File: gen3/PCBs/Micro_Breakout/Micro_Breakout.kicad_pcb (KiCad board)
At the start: 4 copper layers, 0 parts

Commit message: microcontroller breakout board completed!!
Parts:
- added C1: 10uF, Capacitor_SMD:C_0805_2012Metric_Pad1.18x1.45mm_HandSolder, F.Cu at (83.0, 73.5)
- added C12: 10uF, Capacitor_SMD:C_0805_2012Metric_Pad1.18x1.45mm_HandSolder, F.Cu at (84.5, 85.5)
- added C13: 10uF, Capacitor_SMD:C_0805_2012Metric_Pad1.18x1.45mm_HandSolder, F.Cu at (83.5, 89.5)
- added C14: 1uF, Capacitor_SMD:C_0805_2012Metric_Pad1.18x1.45mm_HandSolder, F.Cu at (87.0, 89.5)
- added C15: 10uF, Capacitor_SMD:C_0805_2012Metric_Pad1.18x1.45mm_HandSolder, F.Cu at (76.0, 81.0)
- added C2: 1uF, Capacitor_SMD:C_0805_2012Metric_Pad1.18x1.45mm_HandSolder, F.Cu at (86.0, 73.5)
- added H6: MountingHole, MountingHole:MountingHole_4.3mm_M4, F.Cu at (64.0, 54.5)
- added H7: MountingHole, MountingHole:MountingHole_4.3mm_M4, F.Cu at (64.0, 128.5)
- added H8: MountingHole, MountingHole:MountingHole_4.3mm_M4, F.Cu at (178.5, 54.5)
- added H9: MountingHole, MountingHole:MountingHole_4.3mm_M4, F.Cu at (178.5, 128.5)
- added J1: BlueRobotics Depth Sensor, Imported_Footprints:CONN_SD-43045-005_04_MOL, F.Cu at (134.5, 57.1)
- added J10: Kill Switch, Imported_Footprints:CONN_SD-43045-005_02_MOL, F.Cu at (141.3, 73.9)
- added J11: StarOddi CTD Comms, Imported_Footprints:CONN_SD-43045-005_04_MOL, F.Cu at (147.5, 57.1)
- added J12: LED1, Imported_Footprints:CONN_SD-43045-005_02_MOL, F.Cu at (150.8, 74.0)
- added J13: LED2, Imported_Footprints:CONN_SD-43045-005_02_MOL, F.Cu at (160.3, 74.0)
- added J14: Leak Sensor, Connector_PinHeader_2.54mm:PinHeader_1x03_P2.54mm_Vertical, F.Cu at (155.0, 57.1)
- added J15: Extra I2C #3, Imported_Footprints:CONN_SD-43045-005_04_MOL, F.Cu at (98.0, 88.5)
- added J16: Extra I2C #6, Imported_Footprints:CONN_SD-43045-005_04_MOL, F.Cu at (98.0, 121.5)
- added J17: Extra I2C #5, Imported_Footprints:CONN_SD-43045-005_04_MOL, F.Cu at (98.0, 110.5)
- added J18: Extra I2C #4, Imported_Footprints:CONN_SD-43045-005_04_MOL, F.Cu at (98.0, 99.5)
- added J19: GND Line, Connector_PinHeader_2.54mm:PinHeader_1x10_P2.54mm_Vertical, F.Cu at (74.0, 127.3)
- added J2: Interconnect, Imported_Footprints:SULLINS_SBH11-PBPC-D05-ST-BK, F.Cu at (153.9, 89.3)
- added J20: 3.3V Line, Connector_PinHeader_2.54mm:PinHeader_1x10_P2.54mm_Vertical, F.Cu at (78.0, 127.3)
- added J21: 5V Line, Connector_PinHeader_2.54mm:PinHeader_1x10_P2.54mm_Vertical, F.Cu at (82.0, 127.2)
- added J22: Extra SPI #1, Imported_Footprints:CONN_SD-43045-005_06_MOL, F.Cu at (119.5, 57.0)
- added J23: Extra SPI #2, Imported_Footprints:CONN_SD-43045-005_06_MOL, F.Cu at (119.5, 74.0)
- added J24: Extra SPI #3, Imported_Footprints:CONN_SD-43045-005_06_MOL, F.Cu at (119.5, 91.6)
- added J25: Secondary UART, Imported_Footprints:CONN_SD-43045-005_04_MOL, F.Cu at (134.8, 91.5)
- added J3: External Battery, Connector_AMASS:AMASS_XT60PW-F_1x02_P7.20mm_Horizontal, F.Cu at (83.2, 57.8)
- added J4: Conn_01x24, Connector_PinHeader_2.54mm:PinHeader_1x24_P2.54mm_Vertical, F.Cu at (168.1, 103.6)
- added J5: External I2C, Connector_AMASS:AMASS_XT30PW-F_1x02_P2.50mm_Horizontal, F.Cu at (94.5, 57.6)
- added J6: Conn_01x24, Connector_PinHeader_2.54mm:PinHeader_1x24_P2.54mm_Vertical, F.Cu at (168.0, 126.1)
- added J7: Extra I2C #1, Imported_Footprints:CONN_SD-43045-005_04_MOL, F.Cu at (98.0, 66.5)
- added J8: Extra I2C #2, Imported_Footprints:CONN_SD-43045-005_04_MOL, F.Cu at (98.0, 77.5)
- added J9: Lumen PWM, Imported_Footprints:CONN_SD-43045-005_02_MOL, F.Cu at (131.8, 73.9)
- added Q7: L78M05ABDT-TR, robosub_footprints:TO-252-2_L6.5-W6.1-P4.58-LS10.0-TL, F.Cu at (76.0, 74.0)
- added R1: 0R, Resistor_SMD:R_0805_2012Metric_Pad1.20x1.40mm_HandSolder, F.Cu at (83.0, 96.0)
- added R10: 10k, Resistor_SMD:R_0805_2012Metric_Pad1.20x1.40mm_HandSolder, F.Cu at (104.5, 112.0)
- added R11: 10k, Resistor_SMD:R_0805_2012Metric_Pad1.20x1.40mm_HandSolder, F.Cu at (104.5, 109.0)
- added R2: 10k, Resistor_SMD:R_0805_2012Metric_Pad1.20x1.40mm_HandSolder, F.Cu at (83.0, 99.0)
- added R3: 10k, Resistor_SMD:R_0805_2012Metric_Pad1.20x1.40mm_HandSolder, F.Cu at (87.0, 98.0)
- added R4: 10k, Resistor_SMD:R_0805_2012Metric_Pad1.20x1.40mm_HandSolder, F.Cu at (86.0, 68.5)
- added R5: 10k, Resistor_SMD:R_0805_2012Metric_Pad1.20x1.40mm_HandSolder, F.Cu at (83.0, 68.5)
- added R6: 10k, Resistor_SMD:R_0805_2012Metric_Pad1.20x1.40mm_HandSolder, F.Cu at (104.5, 121.0)
- added R7: 10k, Resistor_SMD:R_0805_2012Metric_Pad1.20x1.40mm_HandSolder, F.Cu at (104.5, 118.0)
- added R8: 10k, Resistor_SMD:R_0805_2012Metric_Pad1.20x1.40mm_HandSolder, F.Cu at (104.5, 115.0)
- added U15: AMS1117-3.3, Package_TO_SOT_SMD:SOT-223-3_TabPin2, F.Cu at (77.0, 88.0)
- added U2: MCP9808_MSOP, Package_SO:MSOP-8_3x3mm_P0.65mm, F.Cu at (84.5, 78.5)
- added U4: BME280, Package_LGA:Bosch_LGA-8_2.5x2.5mm_P0.65mm_ClockwisePinNumbering, F.Cu at (77.0, 97.5)
- added U6: Teensy4.1, Imported_Footprints:Teensy41, F.Cu at (138.8, 114.9)
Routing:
- net GND: track 0.00 -> 379.9 mm
- net +3.3V: track 0.00 -> 364.2 mm, vias 0 -> 7
- net I2C1_SDA: track 0.00 -> 259.3 mm, vias 0 -> 2
- net I2C1_SCL: track 0.00 -> 233.5 mm
- net UART_TX2: track 0.00 -> 214.5 mm
- net +5V: track 0.00 -> 176.1 mm, vias 0 -> 2
- net SPI_SCK: track 0.00 -> 164.6 mm
- net UART_RX2: track 0.00 -> 115.3 mm, vias 0 -> 4
- net UART_TX1: track 0.00 -> 114.2 mm
- net UART_RX1: track 0.00 -> 110.1 mm
- net I2C2_SDA: track 0.00 -> 97.5 mm, vias 0 -> 1
- net SPI_MISO: track 0.00 -> 88.4 mm, vias 0 -> 6
- net SPI_CS3: track 0.00 -> 83.3 mm
- net I2C2_SCL: track 0.00 -> 81.7 mm
- net SPI_MOSI: track 0.00 -> 72.9 mm, vias 0 -> 3
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- added copper zone on B.Cu, net GND
- added copper zone on F.Cu, net GND
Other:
- board outline added: 123.5 x 83 mm
- copper layers 4 -> 2
- board text added: "/\ /**\ /****\ /******\ ||"
- board text added: "3.3V"
- board text added: "5V"
- board text added: "BlueRobotics Depth"
- board text added: "By: Ryota Sato"
- board text added: "Extra I2C"
- board text added: "Extra UART"
- board text added: "GND"
- board text added: "Interconnect"
- board text added: "Kill Switch"
- board text added: "LED1"
- board text added: "LED2"
- board text added: "Leak Sensor"
- board text added: "Microcontroller Breakout Board"
- board text added: "SPI #1"
- board text added: "SPI #2"
- board text added: "SPI #3"
- board text added: "StarOddi"

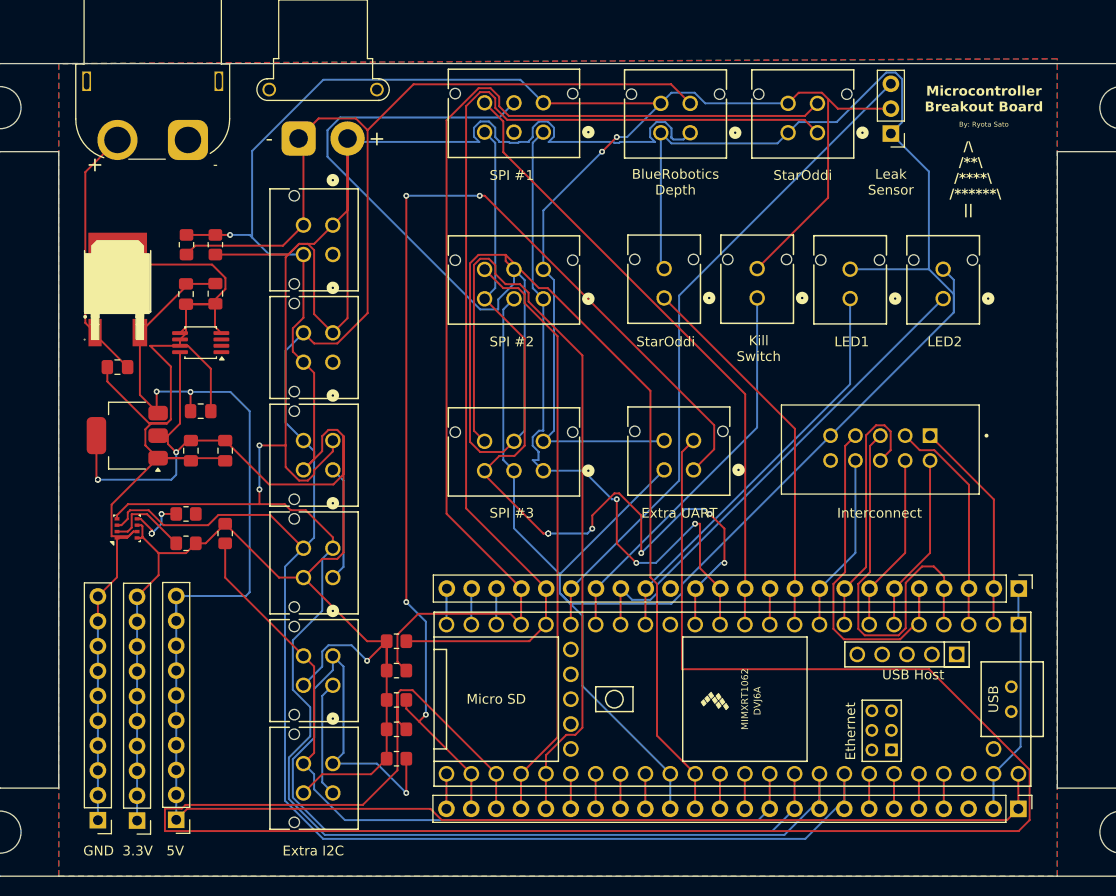
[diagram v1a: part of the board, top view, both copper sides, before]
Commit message: fixed pinout for ribbon
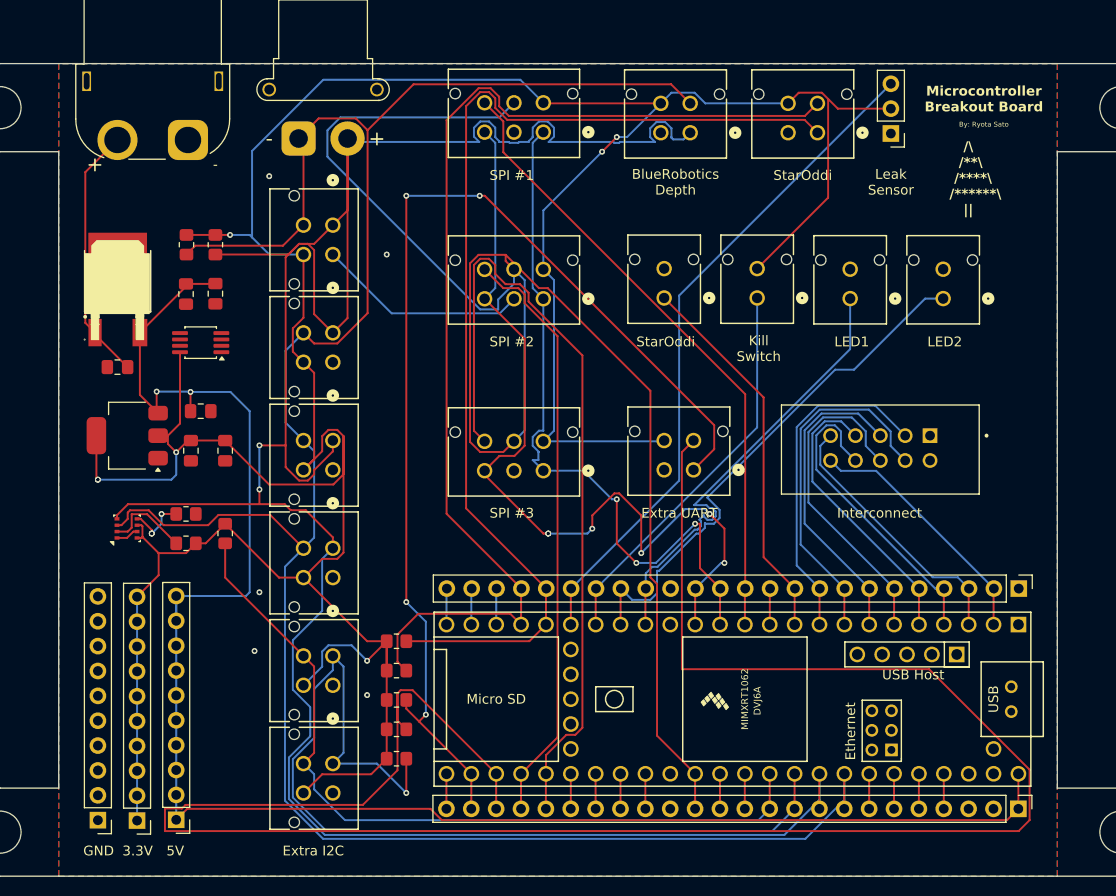
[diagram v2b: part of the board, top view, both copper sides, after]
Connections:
- J2 pad 1: PWM0 -> unconnected-(J2-Pad1)
- J2 pad 10: unconnected-(J2-Pad10) -> PWM0
- J2 pad 2: PWM4 -> GND
- J2 pad 3: PWM1 -> PWM7
- J2 pad 4: PWM5 -> PWM6
- J2 pad 5: PWM2 -> PWM5
- J2 pad 6: PWM6 -> PWM4
- J2 pad 8: PWM7 -> PWM2
- J2 pad 9: GND -> PWM1
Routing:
- net GND: track 379.9 -> 24.0 mm, vias 0 -> 5
- net PWM7: track 18.3 -> 34.4 mm
- net PWM4: track 18.3 -> 34.0 mm
- net PWM5: track 18.3 -> 32.0 mm
- net PWM6: track 26.9 -> 36.4 mm
- net PWM2: track 40.7 -> 32.1 mm
- net PWM3: track 37.6 -> 29.6 mm
- net PWM1: track 22.9 -> 27.5 mm
- net Dled1: track 42.0 -> 46.5 mm
- net Dled2: track 50.3 -> 54.5 mm
- net PWM0: track 22.0 -> 25.8 mm
- net I2C1_SDA: vias 2 -> 3

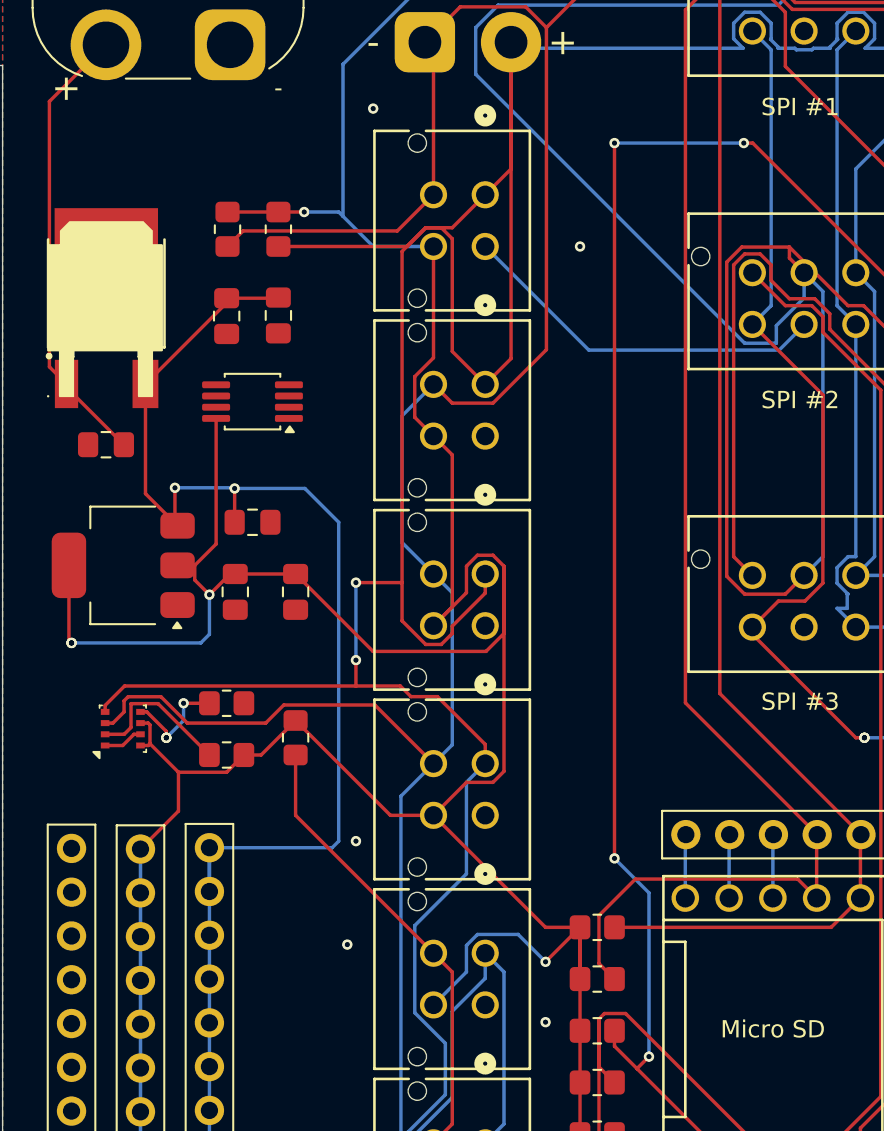
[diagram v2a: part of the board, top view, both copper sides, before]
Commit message: fixed GND plane
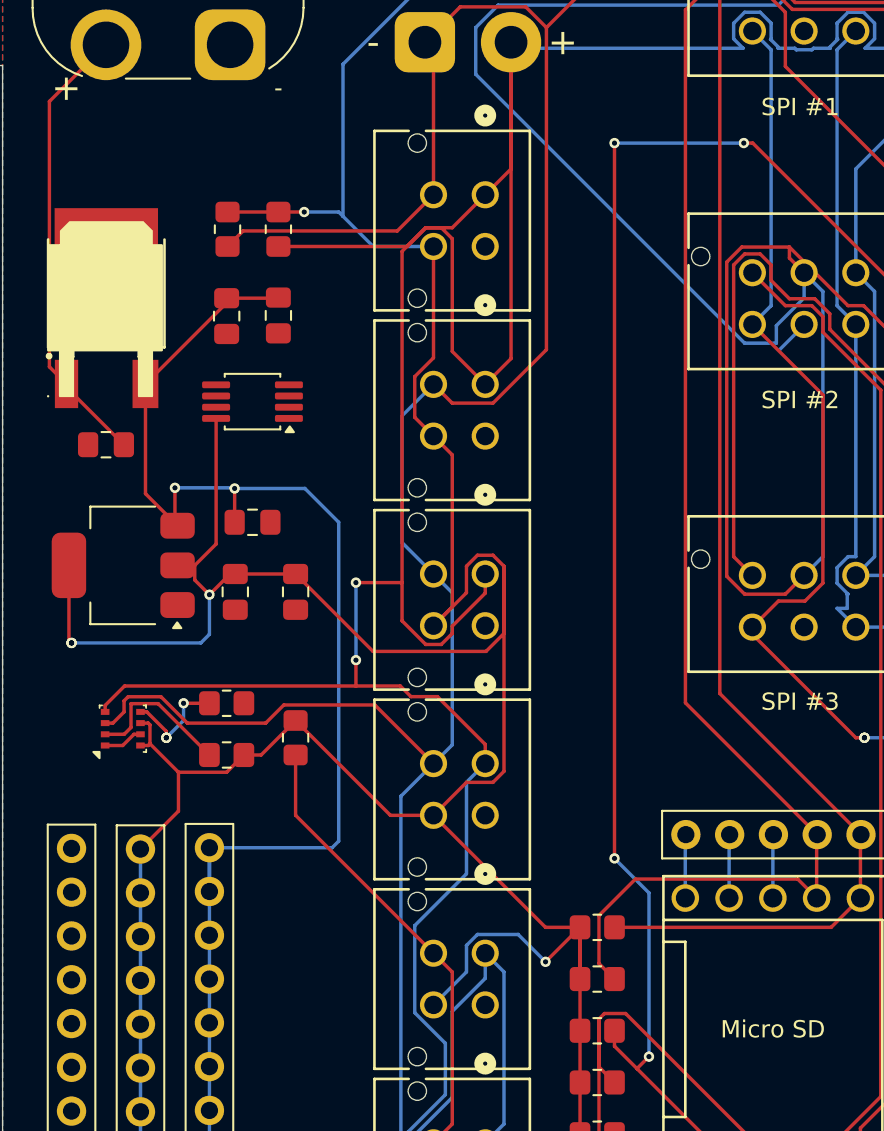
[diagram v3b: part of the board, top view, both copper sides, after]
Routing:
- net GND: track 24.0 -> 4.41 mm, vias 5 -> 0
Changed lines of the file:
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@@
 	)
 	(segment
-		(start 75.95 98.45)
+		(start 77.623 97.8)
 		(end 76.973 98.45)
 		(width 0.2)
@@
 	)
 	(segment
-		(start 76.973 98.45)
+		(start 78 97.8)
 		(end 77.623 97.8)
 		(width 0.2)
@@
 	)
 	(segment
-		(start 77.623 97.8)
-		(end 78 97.8)
+		(start 76.973 98.45)
+		(end 75.95 98.45)
 		(width 0.2)
 		(layer "F.Cu")
-		(net 2)
-	)
-	(via
-		(at 103.5 69.5)
-		(size 0.6)
-		(drill 0.3)
-		(layers "F.Cu" "B.Cu")
-		(free yes)
-		(net 2)
-	)
-	(via
-		(at 101.5 114.5)
-		(size 0.6)
-		(drill 0.3)
-		(layers "F.Cu" "B.Cu")
-		(free yes)
-		(net 2)
-	)
-	(via
-		(at 90 110)
-		(size 0.6)
-		(drill 0.3)
-		(layers "F.Cu" "B.Cu")
-		(free yes)
-		(net 2)
-	)
-	(via
-		(at 90.5 104)
-		(size 0.6)
-		(drill 0.3)
-		(layers "F.Cu" "B.Cu")
-		(free yes)
-		(net 2)
-	)
-	(via
-		(at 91.5 61.5)
-		(size 0.6)
-		(drill 0.3)
-		(layers "F.Cu" "B.Cu")
-		(free yes)
-		(net 2)
-	)
-	(segment
-		(start 115.056201 75.510899)
-		(end 104.0109 75.510899)
-		(width 0.2)
-		(layer "B.Cu")
 		(net 2)
 	)
@@
 		(width 0.2)
 		(layer "B.Cu")
-		(net 2)
-	)
-	(segment
-		(start 104.0109 75.510899)
-		(end 98 69.499999)
-		(width 0.2)
-		(layer "B.Cu")
